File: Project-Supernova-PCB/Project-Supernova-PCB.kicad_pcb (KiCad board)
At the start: 2 copper layers, 99.1 x 87.6 mm, 38 parts, among them J1 Conn_01x04, J10 Conn_01x02, J11 Screw_Terminal_01x02, J12 Screw_Terminal_01x02, J2 Conn_01x04, J3 Conn_01x02, J4 Conn_Coaxial, J5 100k_Thermistor, J6 Screw_Terminal_01x02, J7 Screw_Terminal_01x02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

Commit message: PCB changes, finish Rev1 as ordered
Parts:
- added D1: LED, LED_SMD:LED_1206_3216Metric_Pad1.42x1.75mm_HandSolder, F.Cu at (119.2, 106.0)
- added D2: LED, LED_SMD:LED_1206_3216Metric_Pad1.42x1.75mm_HandSolder, F.Cu at (111.5, 114.9)
- added D3: LED, LED_SMD:LED_1206_3216Metric_Pad1.42x1.75mm_HandSolder, F.Cu at (98.8, 114.9)
- added H5: MountingHole, MountingHole:MountingHole_3mm, F.Cu at (179.7, 92.7)
- added H6: MountingHole, MountingHole:MountingHole_3mm, F.Cu at (179.7, 102.2)
- added J13: Conn_01x03, Connector_PinHeader_2.54mm:PinHeader_1x03_P2.54mm_Vertical, F.Cu at (146.1, 55.9)
- added R10: 3.3k, Resistor_SMD:R_1206_3216Metric_Pad1.30x1.75mm_HandSolder, F.Cu at (98.8, 111.8)
- added R6: 4.7k, Resistor_SMD:R_1206_3216Metric_Pad1.30x1.75mm_HandSolder, F.Cu at (160.3, 62.2)
- added R7: 4.7k, Resistor_SMD:R_1206_3216Metric_Pad1.30x1.75mm_HandSolder, F.Cu at (166.0, 62.2)
- added R8: 1k, Resistor_SMD:R_1206_3216Metric_Pad1.30x1.75mm_HandSolder, F.Cu at (119.1, 109.9)
- added R9: 1k, Resistor_SMD:R_1206_3216Metric_Pad1.30x1.75mm_HandSolder, F.Cu at (111.5, 111.8)
- added TP1: TestPoint, TestPoint:TestPoint_Pad_D3.0mm, F.Cu at (125.5, 54.0)
- added TP2: TestPoint, TestPoint:TestPoint_Pad_D4.0mm, F.Cu at (179.1, 66.0)
- added TP3: TestPoint, TestPoint:TestPoint_Pad_D4.0mm, F.Cu at (179.1, 81.3)
- J4: footprint Connector_Coaxial:SMA_Molex_73251-1153_EdgeMount_Horizontal -> Connector_Coaxial:SMA_Wurth_60312002114503_Vertical
- moved J4 2.93 mm to (89.9, 63.5)
- moved J6 2.54 mm to (138.4, 127.0)
- moved U2 2.54 mm to (163.8, 72.4)
- moved SW1 2.40 mm to (130.2, 126.6)
- moved SW2 2.40 mm to (122.6, 126.6)
- moved J10 1.27 mm to (110.5, 118.1)
- moved J11 1.27 mm to (96.5, 127.0)
- moved J12 1.27 mm to (108.6, 127.0)
- moved J9 1.27 mm to (97.8, 118.1)
- moved R4 0.63 mm to (160.0, 104.8)
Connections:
- U3 pad 28: unconnected-(U3-PB0-Pad28) -> Net-(U3-PB0)
- U5 pad 15: unconnected-(U5-D23/VSPI_MOSI-Pad15) -> Net-(J13-Pin_1)
- U5 pad 23: unconnected-(U5-D25/ADC2_CH8/DAC1-Pad23) -> Net-(J13-Pin_2)
- U5 pad 24: unconnected-(U5-D26/ADC2_CH9/DAC2-Pad24) -> Net-(J13-Pin_3)
- U5 pad 28: unconnected-(U5-D13/ADC2_CH4/TOUCH4/HSPI_MOSI-Pad28) -> /TOUCH4
- U5 pad 3: unconnected-(U5-D15/ADC2_CH3/TOUCH3/HSPI_CS0-Pad3) -> /TOUCH3
- U5 pad 8: unconnected-(U5-D5/VSPI_CS0-Pad8) -> Net-(U5-D5/VSPI_CS0)
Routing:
- net Net-(J13-Pin_1): track 0.00 -> 67.5 mm, vias 0 -> 1
- net /TOUCH3: track 0.00 -> 56.5 mm
- net +BATT: track 69.3 -> 107.1 mm
- net /TOUCH4: track 0.00 -> 37.6 mm, vias 0 -> 2
- net Net-(J13-Pin_2): track 0.00 -> 34.2 mm, vias 0 -> 1
- net Net-(J13-Pin_3): track 0.00 -> 32.5 mm, vias 0 -> 1
- net Net-(U3-PB0): track 0.00 -> 31.2 mm, vias 0 -> 2
- net Net-(U5-D5/VSPI_CS0): track 0.00 -> 29.3 mm, vias 0 -> 1
- net SCL: track 64.7 -> 74.8 mm, vias 1 -> 3
- net SDA: track 50.4 -> 59.5 mm, vias 1 -> 2
- net +3V3: track 18.4 -> 25.9 mm, vias 2 -> 6
- net Net-(D1-A): track 0.00 -> 6.88 mm, vias 0 -> 2
- net Net-(U3-RFIO): track 0.00 -> 6.21 mm
- net Net-(D3-A): track 0.00 -> 3.17 mm
- net Net-(D2-A): track 0.00 -> 3.17 mm
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- removed copper zone on F.Cu, net Net-(U3-RFIO)
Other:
- board text added: "D23"
- board text added: "D25"
- board text added: "D26"
- board text added: "D5 GPIO"
- board text added: "Fabricate on 0.8mm FR4 for RF 50 ohm trace RF Math (v1): - Dielectric Constant = 4.6 (https://jlcpcb.com/impedance) - Calculator: https://www.everythingrf.com/rf-calculators/microstrip-width-calculator - Dielectric Thickness = 0.8 - 0.035*2 = 0.73mm - Track Thickness = 0.035mm, Target Impedance = 50 ohm ==> RF Trace Thickness = 1.29mm RF Math (v2): - Use https://jlcpcb.com/pcb-impedance-calculato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"
- board text added: "GND|V_BATT"
- board text added: "NC"
- board text added: "REV 1 2023-05-21 Balloon Pals"
- board text added: "TOUCH3"
- board text added: "TOUCH4"
- board text added: "Temp #1"
- board text added: "Temp #2"
- board text added: "V_BATT"
- board text removed: "GND|BATT"
- board text removed: "REV 1 2023-05-19 Balloon Pals"
- board text removed: "TEMP SENSE 1"
- board text removed: "TEMP SENSE 2"
- board text removed: "X"

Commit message: Lock in Rev2 Gerber
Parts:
- removed TP2, TP3: TestPoint, TestPoint:TestPoint_Pad_D4.0mm
- added C8: 10u, Capacitor_SMD:C_1206_3216Metric_Pad1.33x1.80mm_HandSolder, F.Cu at (153.2, 116.2)
- added D4: LED, LED_SMD:LED_1206_3216Metric_Pad1.42x1.75mm_HandSolder, F.Cu at (106.2, 105.4)
- added H10: MountingHole, MountingHole:MountingHole_2mm, F.Cu at (182.4, 100.6)
- added H11: MountingHole, MountingHole:MountingHole_2mm, F.Cu at (177.8, 103.6)
- added H12: MountingHole, MountingHole:MountingHole_2mm, F.Cu at (182.4, 103.6)
- added H7: MountingHole, MountingHole:MountingHole_2mm, F.Cu at (182.4, 91.4)
- added H8: MountingHole, MountingHole:MountingHole_2mm, F.Cu at (182.4, 94.5)
- added H9: MountingHole, MountingHole:MountingHole_2mm, F.Cu at (177.8, 100.6)
- added J14: Conn_01x04, Connector_PinHeader_2.54mm:PinHeader_1x04_P2.54mm_Vertical, F.Cu at (179.1, 57.1)
- added J15: Conn_01x04, Connector_PinHeader_2.54mm:PinHeader_1x04_P2.54mm_Vertical, F.Cu at (174.0, 57.1)
- added R11: 10k, Resistor_SMD:R_1206_3216Metric_Pad1.30x1.75mm_HandSolder, F.Cu at (124.0, 114.8)
- added R12: 3.3k, Resistor_SMD:R_1206_3216Metric_Pad1.30x1.75mm_HandSolder, F.Cu at (147.4, 118.0)
- added R13: 4.7k, Resistor_SMD:R_1206_3216Metric_Pad1.30x1.75mm_HandSolder, F.Cu at (133.1, 117.2)
- added R14: 4.7k, Resistor_SMD:R_1206_3216Metric_Pad1.30x1.75mm_HandSolder, F.Cu at (133.1, 114.6)
- added R15: 1k, Resistor_SMD:R_1206_3216Metric_Pad1.30x1.75mm_HandSolder, F.Cu at (106.1, 109.2)
- H5, H6: footprint MountingHole:MountingHole_3mm -> MountingHole:MountingHole_2mm
- J13: value Conn_01x03 -> Conn_01x04; footprint Connector_PinHeader_2.54mm:PinHeader_1x03_P2.54mm_Vertical -> Connector_PinHeader_2.54mm:PinHeader_1x04_P2.54mm_Vertical
- J3: value Conn_01x02 -> Conn_01x04; footprint Connector_PinHeader_2.54mm:PinHeader_1x02_P2.54mm_Vertical -> Connector_PinHeader_2.54mm:PinHeader_1x04_P2.54mm_Vertical
- Q1: footprint Package_TO_SOT_SMD:SOT-23 -> Project-Supernova-Footprint-Lib:SOT-23-MassivePads-HandSolder
- R1: value 4.7k -> 0
- R2, R3: value 4.7k -> 75k
- R4: value 10k -> 18k
- U4: value LM335D -> STDS75DS2F; footprint Package_SO:SOIC-8_3.9x4.9mm_P1.27mm -> Package_SO:MSOP-8_3x3mm_P0.65mm
- moved J3 65.8 mm to (143.3, 55.4), turned to 90 degrees
- moved J13 36.9 mm to (179.1, 72.4), turned to 0 degrees
- moved R1 27.7 mm to (147.4, 114.2)
- moved R5 20.5 mm to (162.8, 105.2)
- moved H6 7.98 mm to (177.8, 94.5)
- moved C2 3.27 mm to (92.2, 104.4)
- moved R4 3.00 mm to (157.1, 105.2)
- moved Q1 2.64 mm to (141.4, 116.1)
- moved H5 2.28 mm to (177.8, 91.4)
- moved U4 1.39 mm to (159.0, 100.0)
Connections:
- J13 pad 1: Net-(J13-Pin_1) -> +BATT
- J13 pad 2: Net-(J13-Pin_2) -> +BATT
- J13 pad 3: Net-(J13-Pin_3) -> +BATT
- J3 pad 1: GPS_UART_MISO -> Net-(J3-Pin_1)
- J3 pad 2: GPS_UART_MOSI -> Net-(J3-Pin_2)
- Q1 pad 1: HEATER_EN -> Net-(Q1-G)
- R1 pad 1: +3V3 -> HEATER_EN
- R1 pad 2: TEMP_SENSE_ONBOARD -> Net-(Q1-G)
- SW1 pad 1: GND -> Net-(SW1-A)
- SW1 pad 3: +3V3 -> Net-(SW1-C)
- U4 pad 1: unconnected-(U4-NC-Pad1) -> SDA
- U4 pad 2: unconnected-(U4-NC-Pad2) -> SCL
- U4 pad 5: unconnected-(U4-ADJ-Pad5) -> GND
- U4 pad 6: unconnected-(U4-NC-Pad6) -> GND
- U4 pad 7: unconnected-(U4-NC-Pad7) -> GND
- U4 pad 8: TEMP_SENSE_ONBOARD -> +3V3
- U5 pad 10: unconnected-(U5-D19/VSPI_MISO-Pad10) -> Net-(J3-Pin_1)
- U5 pad 15: Net-(J13-Pin_1) -> Net-(J3-Pin_2)
- U5 pad 16: unconnected-(U5-EN-Pad16) -> Net-(U5-EN)
- U5 pad 19: TEMP_SENSE_ONBOARD -> BATT_SENSE
- U5 pad 20: TEMP_V+ -> Net-(J3-Pin_4)
- U5 pad 23: Net-(J13-Pin_2) -> TEMP_V+
- U5 pad 24: Net-(J13-Pin_3) -> DHT_DATA
- U5 pad 25: BATT_SENSE -> Net-(J3-Pin_3)
- U5 pad 27: DHT_DATA -> unconnected-(U5-D12/ADC2_CH5/TOUCH5/HSPI_MISO-Pad27)
- U5 pad 28: /TOUCH4 -> GPS_UART_MOSI
- U5 pad 3: /TOUCH3 -> unconnected-(U5-D15/ADC2_CH3/TOUCH3/HSPI_CS0-Pad3)
- U5 pad 4: GPS_UART_MOSI -> unconnected-(U5-D2/ADC2_CH2/TOUCH2-Pad4)
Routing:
- net Net-(J13-Pin_1): track 67.5 -> 0.00 mm, vias 1 -> 0
- net Net-(J3-Pin_2): track 0.00 -> 57.1 mm
- net /TOUCH3: track 56.5 -> 0.00 mm
- net +BATT: track 107.1 -> 163.2 mm
- net Net-(J3-Pin_4): track 0.00 -> 54.9 mm, vias 0 -> 3
- net HEATER_EN: track 41.3 -> 93.8 mm, vias 1 -> 2
- net Net-(J3-Pin_3): track 0.00 -> 46.1 mm, vias 0 -> 1
- net Net-(J3-Pin_1): track 0.00 -> 44.1 mm
- net /TOUCH4: track 37.6 -> 0.00 mm, vias 2 -> 0
- net Net-(J13-Pin_2): track 34.2 -> 0.00 mm, vias 1 -> 0
- net GPS_UART_MISO: track 48.3 -> 14.3 mm, vias 2 -> 0
- net Net-(J13-Pin_3): track 32.5 -> 0.00 mm, vias 1 -> 0
- net SCL: track 74.8 -> 106.1 mm, vias 3 -> 4
- net BATT_SENSE: track 45.3 -> 14.4 mm, vias 1 -> 0
- net SDA: track 59.5 -> 86.7 mm, vias 2 -> 3
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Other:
- board text added: "D19"
- board text added: "D27"
- board text added: "D35"
- board text added: "HEATER"
- board text added: "LoRa Module"
- board text added: "OFF | ON"
- board text added: "PWR"
- board text added: "READY"
- board text added: "REV 2 2023-07-22 Balloon Pals"
- board text added: "SIT | FLY"
- board text removed: "D25"
- board text removed: "D26"
- board text removed: "GPS_MISO"
- board text removed: "GPS_MOSI"
- board text removed: "OFF | ON (PWR)"
- board text removed: "REV 1 2023-05-21 Balloon Pals"
- board text removed: "SIT | FLY (RTF)"
- board text removed: "TOUCH3"
- board text removed: "TOUCH4"

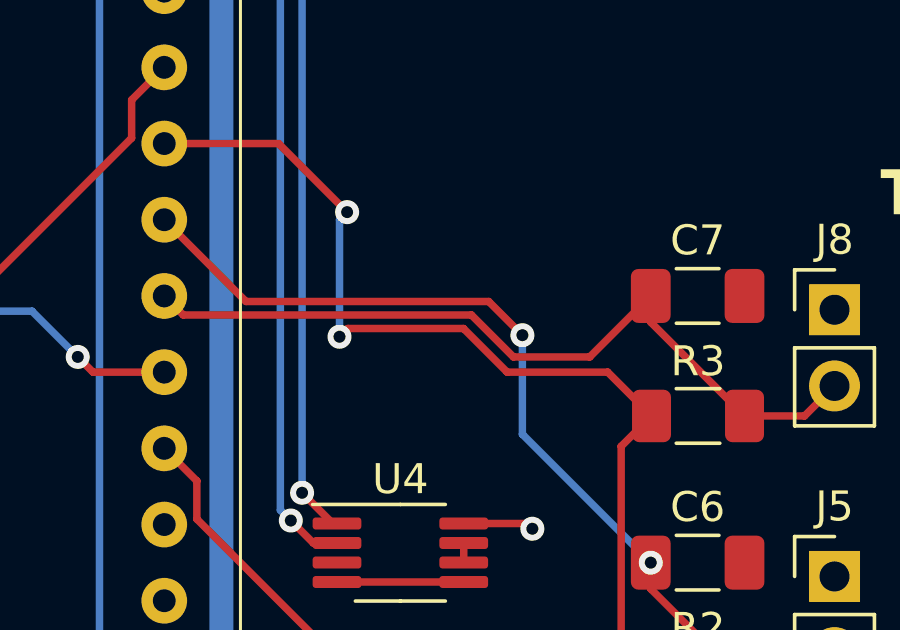
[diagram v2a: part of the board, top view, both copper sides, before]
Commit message: Fix DRC, republish V2
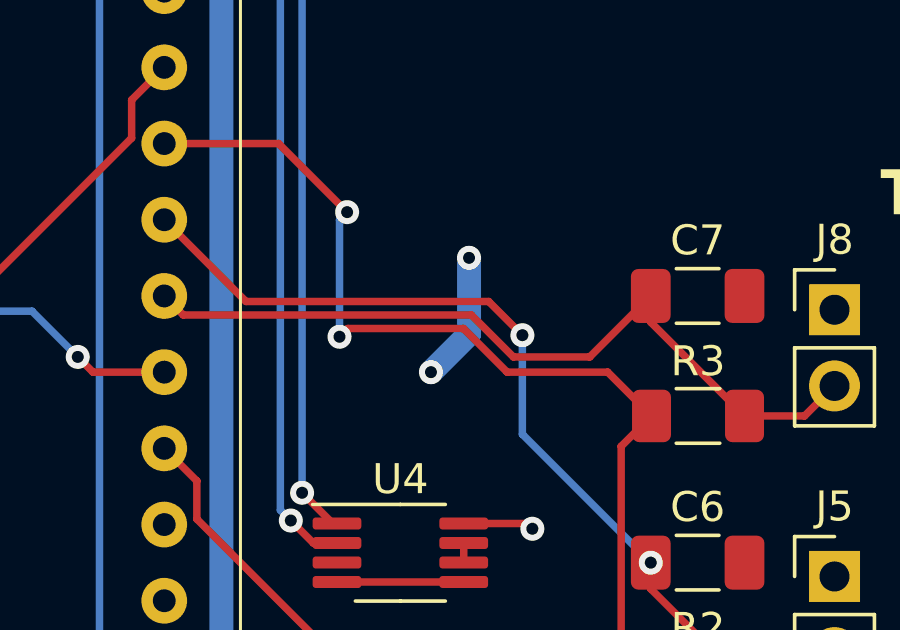
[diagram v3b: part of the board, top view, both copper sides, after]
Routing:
- net GND: track 10.8 -> 15.2 mm, vias 27 -> 29
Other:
- board text added: "Red = Front = GND Blue = Back = 3V3"
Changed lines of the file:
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@@
     (effects (font (size 1.5 1.5) (thickness 0.3) bold))
+  )
+  (gr_text "Red = Front = GND\nBlue = Back = 3V3" (at 194.31 87.63) (layer "Cmts.User")
+    (effects (font (size 2 2) (thickness 0.3)) (justify left bottom))
   )
   (gr_text "Fabricate on 0.8mm FR4 for RF 50 ohm trace\n\nRF Math (v1):\n- Dielectric Constant = 4.6 (https://jlcpcb.com/impedance)\n- Calculator: https://www.everythingrf.com/rf-calculators/microstrip-width-calculator\n- Dielectric Thickness = 0.8 - 0.035*2 = 0.73mm\n- Track Thickness = 0.035mm, Target Impedance = 50 ohm\n==> RF Trace Thickness = 1.29mm\n\nRF Math (v2):\n- Use https://jlcpcb.com/pcb-impedance-calculator/\n- 2 Layers, 0.8 mm Board\n==> 50 ohm, Coplanar Single Ended, with 1mm Clearance -> 1.15mm Trace Width\n- 50 ohm, Single Ended Non-Coplanar   -> 1.20mm Trace Width" (at 20.32 194.945) (layer "Cmts.User")
@@
   (via (at 97.155 53.975) (size 0.8) (drill 0.4) (layers "F.Cu" "B.Cu") (free) (net 2))
   (via (at 91.44 70.485) (size 0.8) (drill 0.4) (layers "F.Cu" "B.Cu") (free) (net 2))
+  (via (at 160.02 93.98) (size 0.8) (drill 0.4) (layers "F.Cu" "B.Cu") (net 2))
+  (via (at 161.29 90.17) (size 0.8) (drill 0.4) (layers "F.Cu" "B.Cu") (net 2))
+  (segment (start 161.29 92.71) (end 160.02 93.98) (width 0.8) (layer "B.Cu") (net 2))
+  (segment (start 161.29 90.17) (end 161.29 92.71) (width 0.8) (layer "B.Cu") (net 2))
   (segment (start 171.4725 103.33) (end 173.4725 103.33) (width 0.25) (layer "F.Cu") (net 3))
   (segment (start 163.068 92.7475) (end 161.9455 91.625) (width 0.25) (layer "F.Cu") (net 3))
